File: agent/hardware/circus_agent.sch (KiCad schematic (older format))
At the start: 2 parts

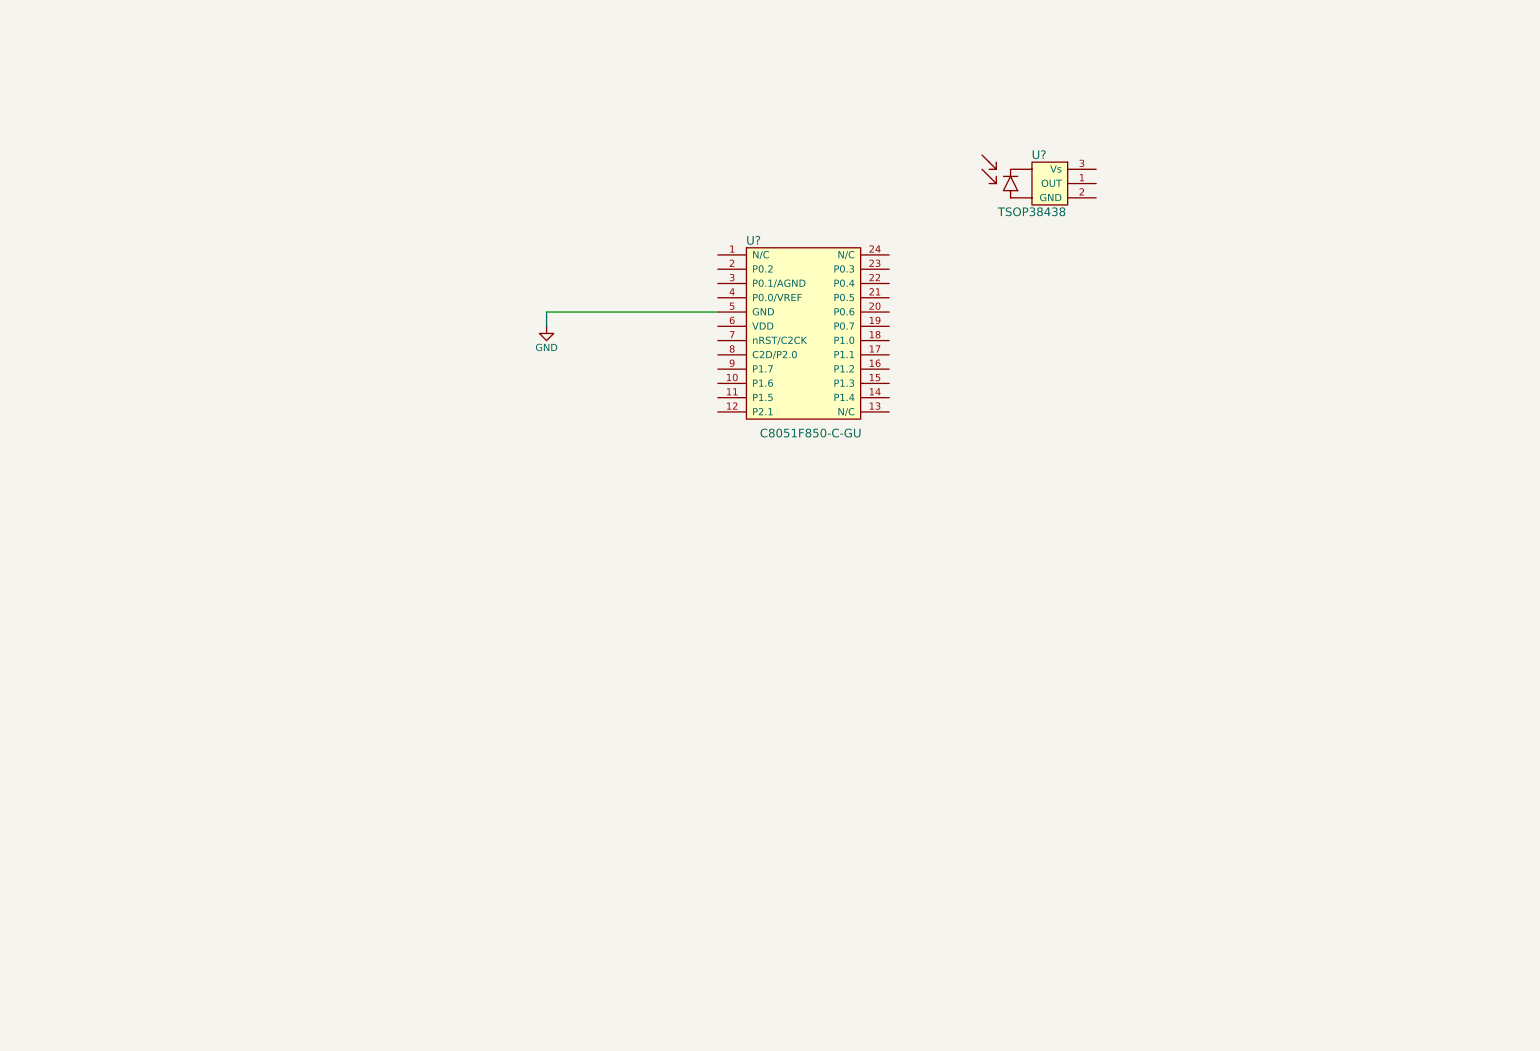
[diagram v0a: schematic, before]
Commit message: added highside switch
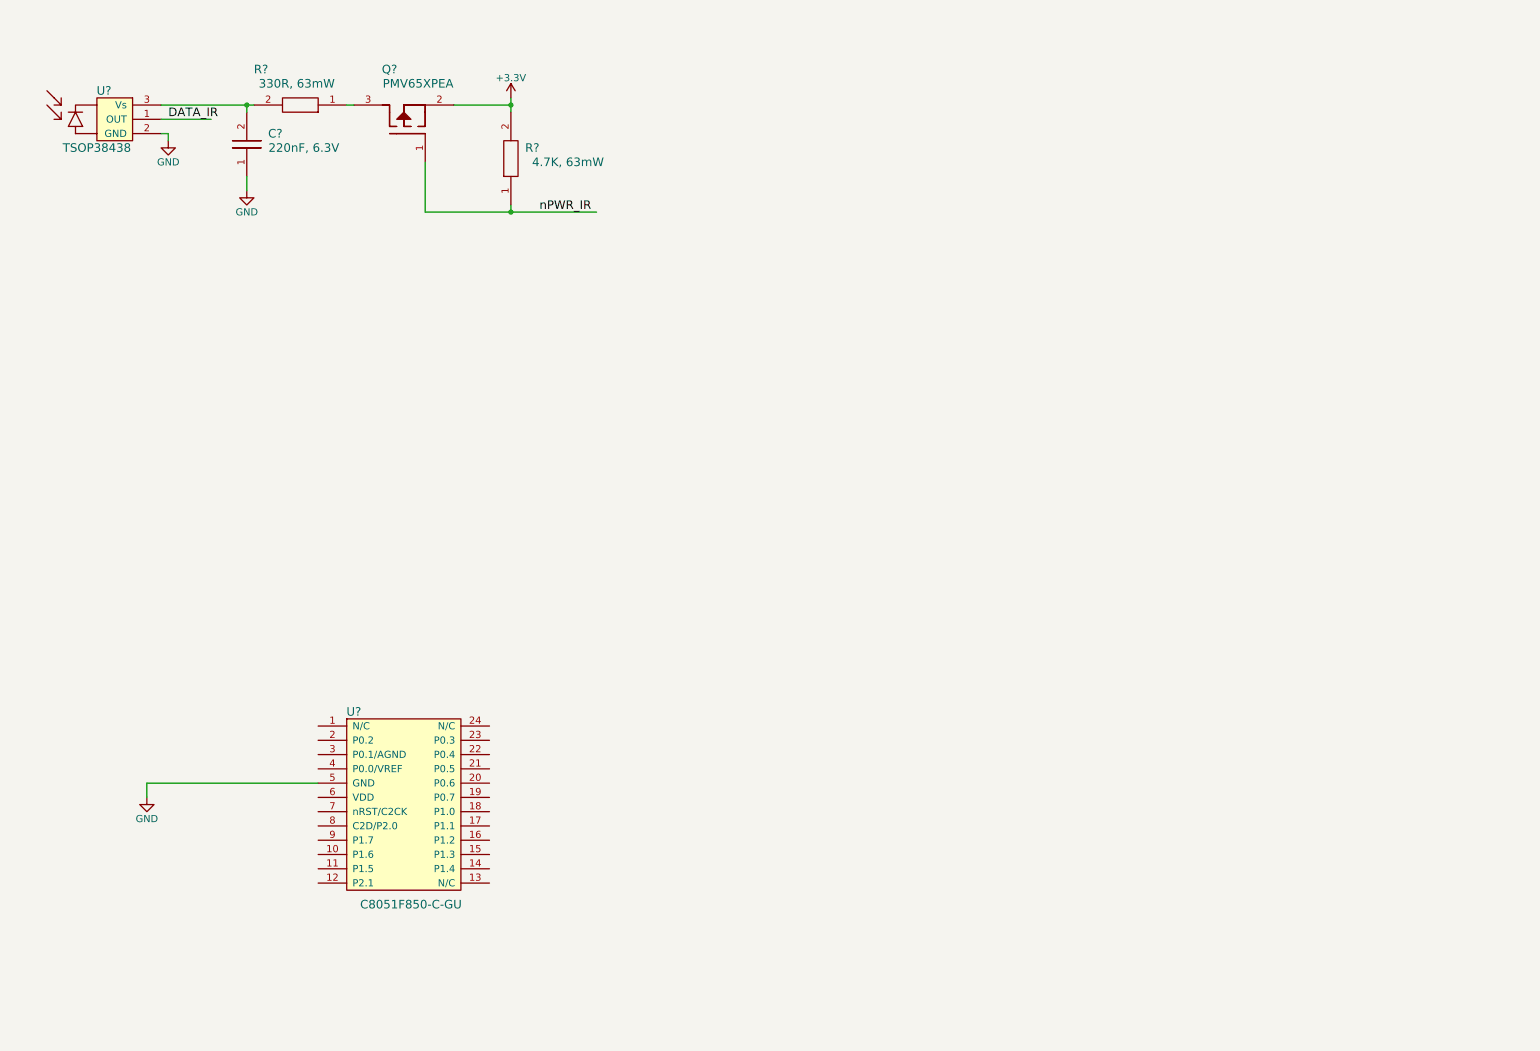
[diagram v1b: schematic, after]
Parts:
- added C?: 220nF, 6.3V, symbol MC0402X224K6R3CT
- added Q?: PMV65XPEA, symbol PMV65XPEA
- added R?: 330R, 63mW, symbol CRCW0402330RFKED
- added R?: 4.7K, 63mW, symbol CRCW0402330RFKED
- U?: Man (none) -> SiLabs; PartNum (none) -> C8051F850-C-GU
- U?: Man (none) -> VISHAY; PartNum (none) -> TSOP38438
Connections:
- net labels added: +3.3V, DATA_IR, nPWR_IR
- wire segments 2 -> 14
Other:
- moved on the sheet: U?
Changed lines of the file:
@@
 LIBS:valves
 LIBS:circus_agent
+LIBS:circus_agent-cache
 EELAYER 25 0
 EELAYER END
@@
 L C8051F850-C-GU U?
 U 1 1 5B327CEA
-P 5500 3150
-F 0 "U?" H 5750 4200 60  0000 C CNN
-F 1 "C8051F850-C-GU" H 6150 2850 60  0000 C CNN
-F 2 "" H 5500 3150 60  0001 C CNN
-F 3 "" H 5500 3150 60  0001 C CNN
-	1    5500 3150
+P 2700 6450
+F 0 "U?" H 2950 7500 60  0000 C CNN
+F 1 "C8051F850-C-GU" H 3350 6150 60  0000 C CNN
+F 2 "" H 2700 6450 60  0001 C CNN
+F 3 "" H 2700 6450 60  0001 C CNN
+F 4 "SiLabs" H 2700 6450 60  0001 C CNN "Man"
+F 5 "C8051F850-C-GU" H 2700 6450 60  0001 C CNN "PartNum"
+	1    2700 6450
 	1    0    0    -1
 $EndComp
 $Comp
-L GND #PWR?
+L GND #PWR01
 U 1 1 5B327D75
-P 4300 2700
-F 0 "#PWR?" H 4300 2450 50  0001 C CNN
-F 1 "GND" H 4300 2550 50  0000 C CNN
-F 2 "" H 4300 2700 50  0001 C CNN
-F 3 "" H 4300 2700 50  0001 C CNN
-	1    4300 2700
+P 1500 6000
+F 0 "#PWR01" H 1500 5750 50  0001 C CNN
+F 1 "GND" H 1500 5850 50  0000 C CNN
+F 2 "" H 1500 6000 50  0001 C CNN
+F 3 "" H 1500 6000 50  0001 C CNN
+	1    1500 6000
 	1    0    0    -1
 $EndComp
 Wire Wire Line
-	5500 2600 4300 2600
+	2700 5900 1500 5900
 Wire Wire Line
-	4300 2600 4300 2700
+	1500 5900 1500 6000
 $Comp
 L TSOP38438 U?
 U 1 1 5B328025
-P 7350 1950
-F 0 "U?" H 7750 2400 60  0000 C CNN
-F 1 "TSOP38438" H 7700 2000 60  0000 C CNN
-F 2 "" H 7700 1900 60  0001 C CNN
-F 3 "" H 7700 1900 60  0001 C CNN
-	1    7350 1950
+P 800 1500
+F 0 "U?" H 1200 1950 60  0000 C CNN
+F 1 "TSOP38438" H 1150 1550 60  0000 C CNN
+F 2 "" H 1150 1450 60  0001 C CNN
+F 3 "" H 1150 1450 60  0001 C CNN
+F 4 "VISHAY" H 800 1500 60  0001 C CNN "Man"
+F 5 "TSOP38438" H 800 1500 60  0001 C CNN "PartNum"
+	1    800  1500
 	1    0    0    -1
 $EndComp
+$Comp
+L MC0402X224K6R3CT C?
+U 1 1 5B32A540
+P 2100 1650
+F 0 "C?" H 2400 1950 60  0000 C CNN
+F 1 "220nF, 6.3V" H 2600 1850 60  0000 C CNN
+F 2 "" H 2100 1650 60  0001 C CNN
+F 3 "" H 2100 1650 60  0001 C CNN
+F 4 "MULTICOMP" H 2100 1650 60  0001 C CNN "Man"
+F 5 "MC0402X224K6R3CT " H 2100 1650 60  0001 C CNN "PartNum"
+	1    2100 1650
+	1    0    0    -1
+$EndComp
+Wire Wire Line
+	2200 1200 2200 1150
+Wire Wire Line
+	1600 1150 2250 1150
+Wire Wire Line
+	2200 1650 2200 1750
+Wire Wire Line
+	1650 1350 1600 1350
+Text Label 1650 1250 0    60   ~ 0
+DATA_IR
+$Comp
+L GND #PWR02
+U 1 1 5B32A820
+P 1650 1400
+F 0 "#PWR02" H 1650 1150 50  0001 C CNN
+F 1 "GND" H 1650 1250 50  0000 C CNN
+F 2 "" H 1650 1400 50  0001 C CNN
+F 3 "" H 1650 1400 50  0001 C CNN
+	1    1650 1400
+	1    0    0    -1
+$EndComp
+$Comp
+L GND #PWR03
+U 1 1 5B32A855
+P 2200 1750
+F 0 "#PWR03" H 2200 1500 50  0001 C CNN
+F 1 "GND" H 2200 1600 50  0000 C CNN
+F 2 "" H 2200 1750 50  0001 C CNN
+F 3 "" H 2200 1750 50  0001 C CNN
+	1    2200 1750
+	1    0    0    -1
+$EndComp
+Wire Wire Line
+	1650 1350 1650 1400
+$Comp
+L CRCW0402330RFKED R?
+U 1 1 5B32A963
+P 2900 1200
+F 0 "R?" V 3200 1800 60  0000 C CNN
+F 1 "330R, 63mW " V 3100 1550 60  0000 C CNN
+F 2 "" H 2900 1200 60  0001 C CNN
+F 3 "" H 2900 1200 60  0001 C CNN
+F 4 "VISHAY" V 2900 1200 60  0001 C CNN "Man"
+F 5 "CRCW0402330RFKED " V 2900 1200 60  0001 C CNN "PartNum"
+	1    2900 1200
+	0    -1   -1   0
+$EndComp
+Connection ~ 2200 1150
+$Comp
+L PMV65XPEA Q?
+U 1 1 5B32B2F5
+P 3650 1550
+F 0 "Q?" V 4300 2000 60  0000 C CNN
+F 1 "PMV65XPEA" V 4200 1800 60  0000 C CNN
+F 2 "" H 3650 1450 60  0001 C CNN
+F 3 "" H 3650 1450 60  0001 C CNN
+F 4 "NXP" V 3650 1550 60  0001 C CNN "Man"
+F 5 "PMV65XPEA" V 3650 1550 60  0001 C CNN "PartNum"
+	1    3650 1550
+	0    -1   -1   0
+$EndComp
+$Comp
+L CRCW0402330RFKED R?
+U 1 1 5B32B5C3
+P 4000 1850
+F 0 "R?" H 4200 2250 60  0000 C CNN
+F 1 "4.7K, 63mW " H 4450 2150 60  0000 C CNN
+F 2 "" H 4000 1850 60  0001 C CNN
+F 3 "" H 4000 1850 60  0001 C CNN
+F 4 "VISHAY" V 4000 1850 60  0001 C CNN "MULTICOMP"
+F 5 "MCMR04X4701FTL" V 4000 1850 60  0001 C CNN "PartNum"
+	1    4000 1850
+	1    0    0    -1
+$EndComp
+Wire Wire Line
+	3650 1150 4050 1150
+Wire Wire Line
+	4050 1100 4050 1200
+$Comp
+L +3.3V #PWR?
+U 1 1 5B32B85B
+P 4050 1100
+F 0 "#PWR?" H 4050 950 50  0001 C CNN
+F 1 "+3.3V" H 4050 1240 50  0000 C CNN
+F 2 "" H 4050 1100 50  0001 C CNN
+F 3 "" H 4050 1100 50  0001 C CNN
+	1    4050 1100
+	1    0    0    -1
+$EndComp
+Connection ~ 4050 1150
+Wire Wire Line
+	4050 1850 4050 1900
+Wire Wire Line
+	3450 1900 4650 1900
+Wire Wire Line
+	3450 1900 3450 1550
+Wire Wire Line
+	1600 1250 1950 1250
+Wire Wire Line
+	2900 1150 2950 1150
+Connection ~ 4050 1900
+Text Label 4250 1900 0    60   ~ 0
+nPWR_IR
 $EndSCHEMATC

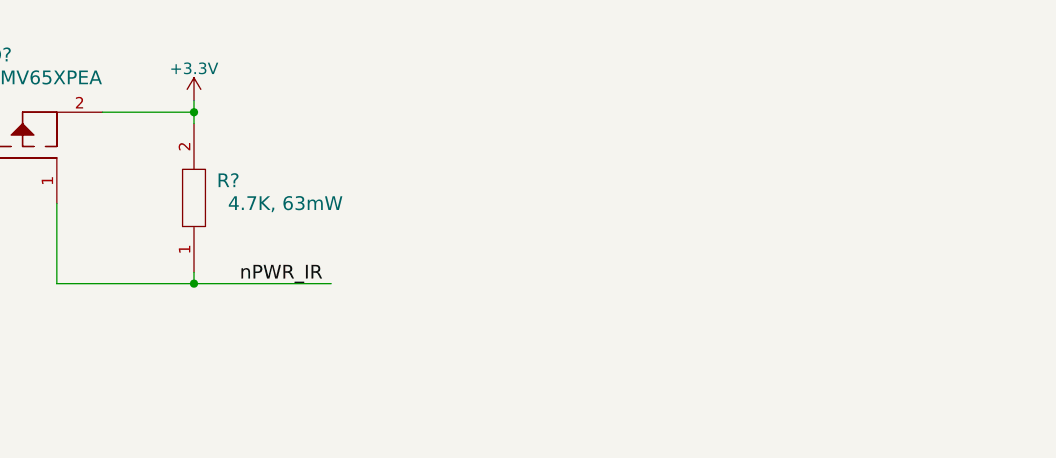
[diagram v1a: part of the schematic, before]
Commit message: Added supercap and power rails
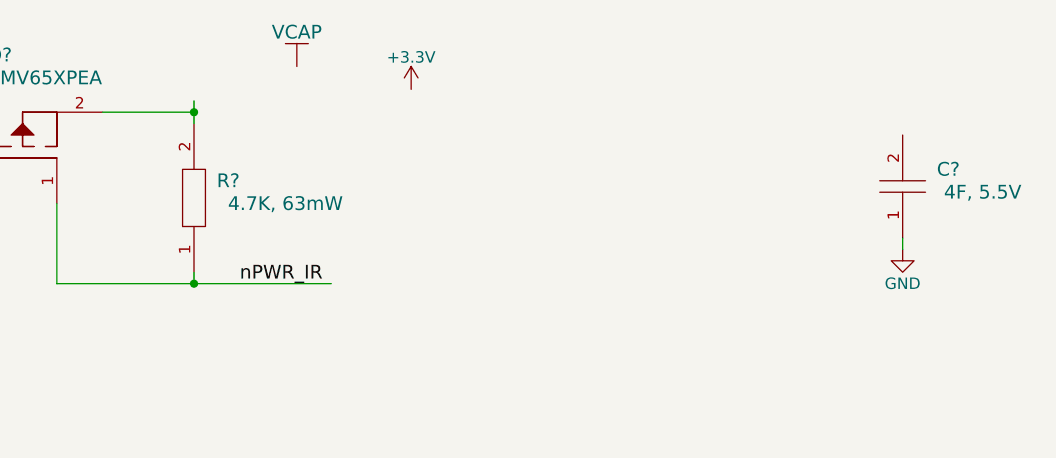
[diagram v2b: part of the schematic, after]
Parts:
- added C?: 4F, 5.5V, symbol SuperCap
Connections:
- net labels added: VCAP
- wire segments 14 -> 15
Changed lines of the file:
@@
 Wire Wire Line
 	4050 1100 4050 1200
-$Comp
-L +3.3V #PWR?
-U 1 1 5B32B85B
-P 4050 1100
-F 0 "#PWR?" H 4050 950 50  0001 C CNN
-F 1 "+3.3V" H 4050 1240 50  0000 C CNN
-F 2 "" H 4050 1100 50  0001 C CNN
-F 3 "" H 4050 1100 50  0001 C CNN
-	1    4050 1100
-	1    0    0    -1
-$EndComp
 Connection ~ 4050 1150
 Wire Wire Line
@@
 Text Label 4250 1900 0    60   ~ 0
 nPWR_IR
+$Comp
+L SuperCap C?
+U 1 1 5B32B674
+P 7050 1700
+F 0 "C?" H 7350 2000 60  0000 C CNN
+F 1 "4F, 5.5V" H 7500 1900 60  0000 C CNN
+F 2 "" H 7050 1700 60  0001 C CNN
+F 3 "" H 7050 1700 60  0001 C CNN
+F 4 "ebay_pp_562" H 7050 1700 60  0001 C CNN "Man"
+F 5 "?" H 7050 1700 60  0001 C CNN "PartNum"
+	1    7050 1700
+	1    0    0    -1
+$EndComp
+$Comp
+L GND #PWR?
+U 1 1 5B32B7AB
+P 7150 1750
+F 0 "#PWR?" H 7150 1500 50  0001 C CNN
+F 1 "GND" H 7150 1600 50  0000 C CNN
+F 2 "" H 7150 1750 50  0001 C CNN
+F 3 "" H 7150 1750 50  0001 C CNN
+	1    7150 1750
+	1    0    0    -1
+$EndComp
+Wire Wire Line
+	7150 1700 7150 1750
+$Comp
+L VCAP #PWR??
+U 1 1 5B333F06
+P 4450 950
+F 0 "#PWR??" H 4750 1100 60  0001 C CNN
+F 1 "VCAP" H 4500 1100 60  0000 C CNN
+F 2 "" H 4450 950 60  0001 C CNN
+F 3 "" H 4450 950 60  0001 C CNN
+	1    4450 950
+	1    0    0    -1
+$EndComp
+$Comp
+L +3.3V #PWR?
+U 1 1 5B3346B1
+P 5000 1050
+F 0 "#PWR?" H 5000 900 50  0001 C CNN
+F 1 "+3.3V" H 5000 1190 50  0000 C CNN
+F 2 "" H 5000 1050 50  0001 C CNN
+F 3 "" H 5000 1050 50  0001 C CNN
+	1    5000 1050
+	1    0    0    -1
+$EndComp
 $EndSCHEMATC

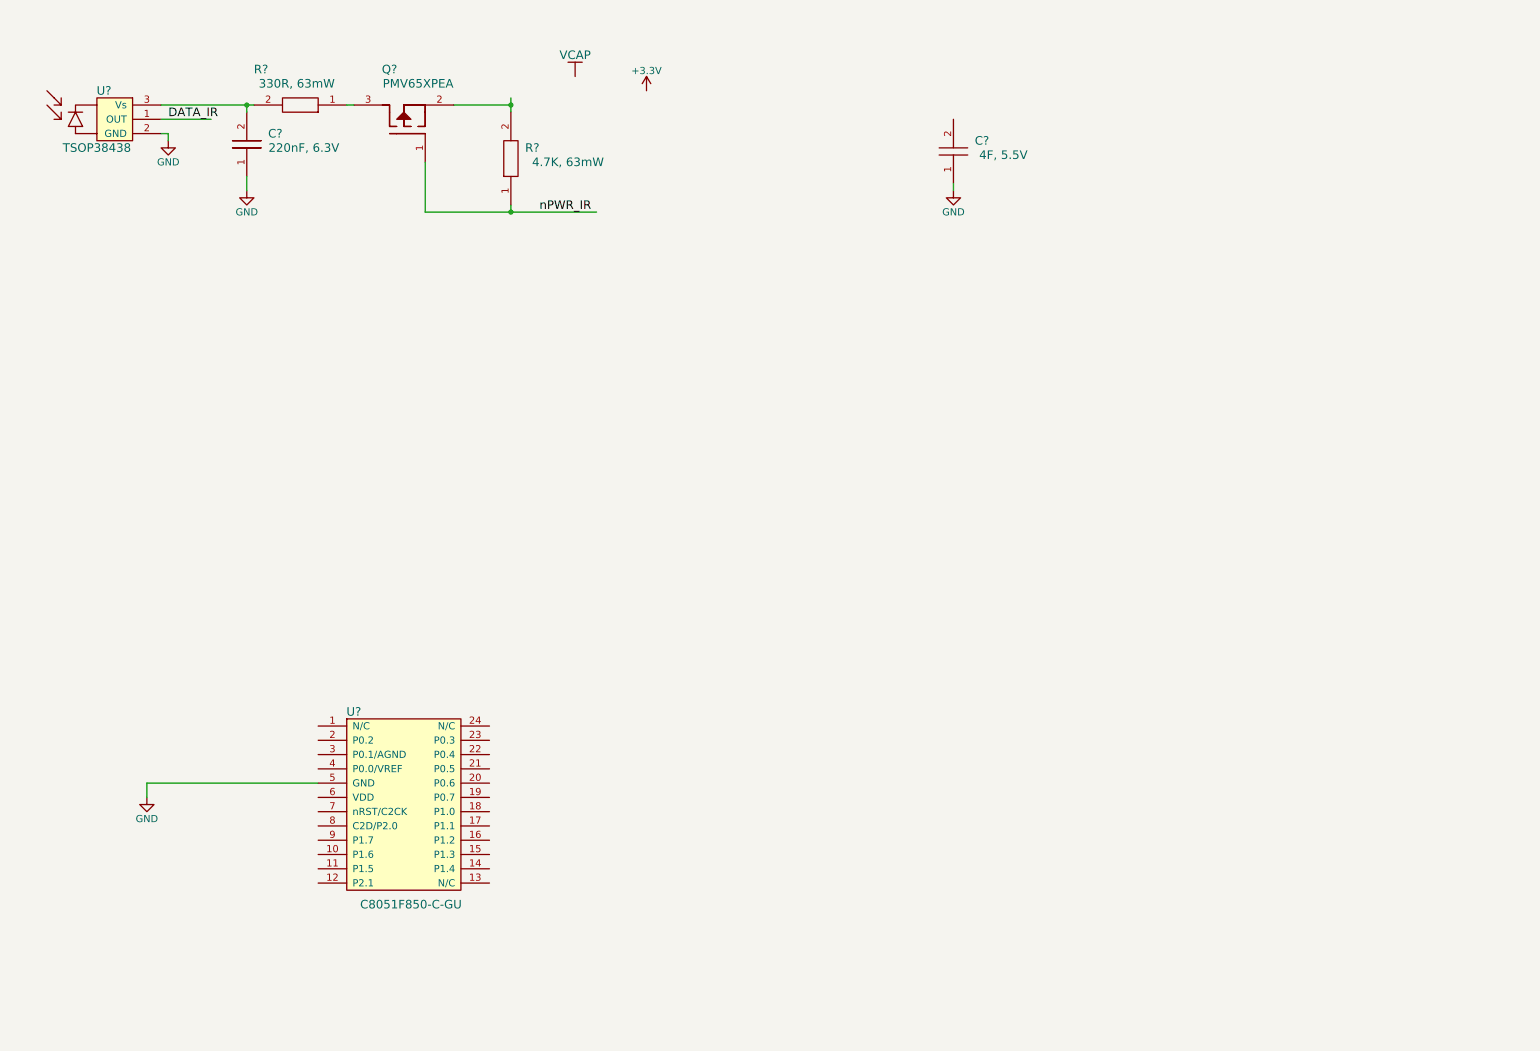
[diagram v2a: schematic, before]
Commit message: Added h bridge and nmos
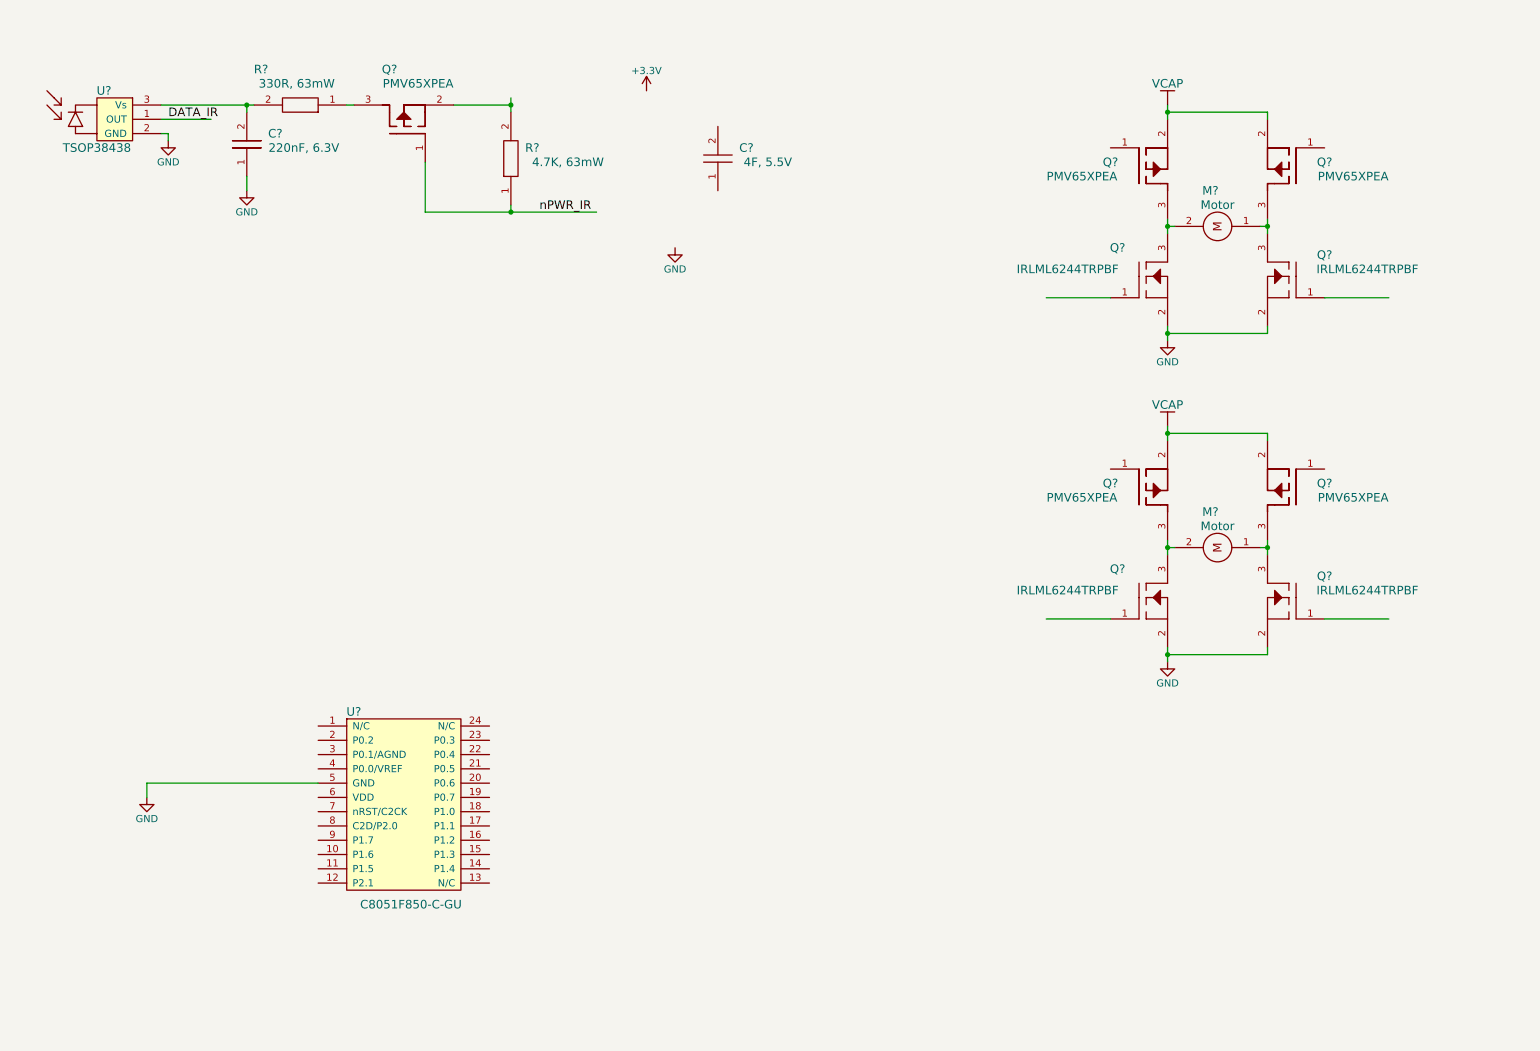
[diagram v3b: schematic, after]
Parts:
- added M? (x2): Motor, symbol Motor
- added Q? (x4): PMV65XPEA, symbol PMV65XPEA
- added Q? (x4): IRLML6244TRPBF, symbol IRLML6244TRPBF
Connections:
- wire segments 15 -> 49
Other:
- moved on the sheet: C?
